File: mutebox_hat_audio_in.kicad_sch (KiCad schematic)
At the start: 23 parts, among them J1 GPIO, U1 CAT24C256, U2 74LVC157, U3 PCM1862DBT

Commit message: Fixed some connections and global labels
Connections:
- net GPIO18/PCM.CLK is gone; now on net I2S_BCLK: J1.12 (Pin_12), U2.4 (Za)
- net ADC_SDOUT: now also U2.10 (I1c)
- net GND: no longer U2.10 (I1c), U2.6 (I1b)
- net GPIO24: no longer U2.1 (S)
- net I2S_BCLK: no longer U2.2 (I0a), U3.17 (BCK)
- net I2S_LRCLK: now also U2.7 (Zb); no longer U2.5 (I0b), U3.16 (LRCK)
- net I2S_SDIN: now also J1.35 (Pin_35); no longer U2.3 (I1a)
- removed net GPIO19/PCM.FS: J1.35 (Pin_35), U2.7 (Zb)
- net GPIO20/PCM.DIN renamed I2S_DOUT
- net GPIO23_OPT_LOCK renamed SRC_SEL
- net SRC_SEL: now also U2.1 (S)
- net SPDIF_SDOUT renamed TOSLINK_DOUT
- new net ADC_BCLK: U2.3 (I1a), U3.17 (BCK)
- new net ADC_LRCLK: U2.6 (I1b), U3.16 (LRCK)
- new net TOSLINK_BCLK: U2.2 (I0a)
- new net TOSLINK_LRCK: U2.5 (I0b)
- no-connect marks 32 -> 33
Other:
- moved on the sheet: C8, J_R_IN1

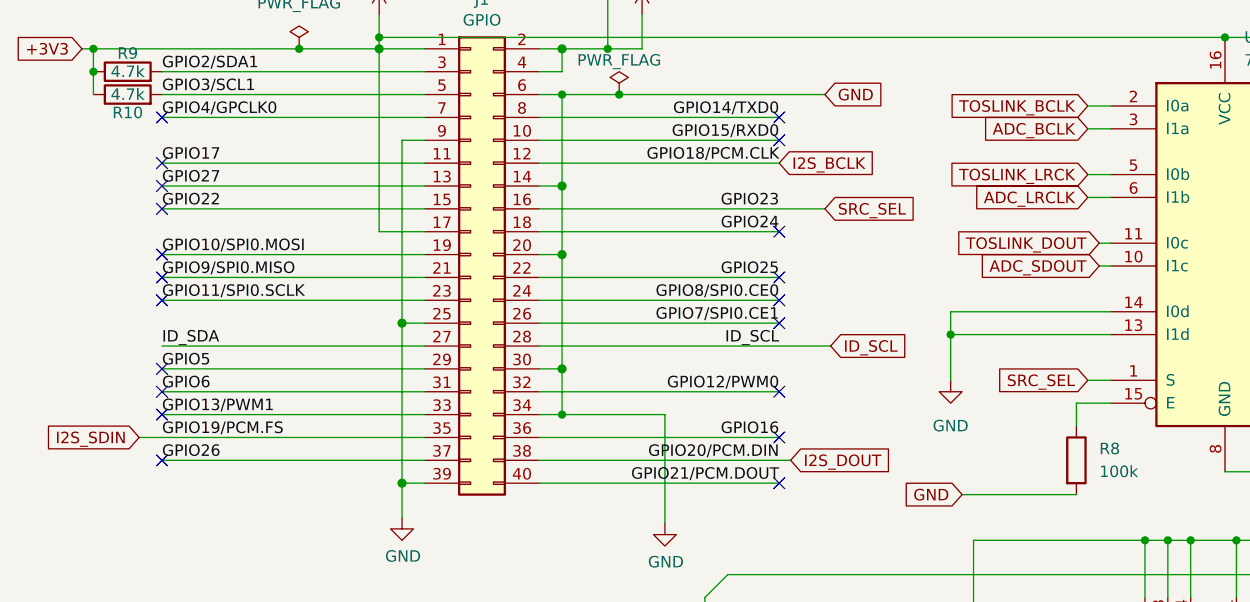
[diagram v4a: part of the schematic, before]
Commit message: Fixed power/caps for TOSLINK.  Got ERC down to warnings
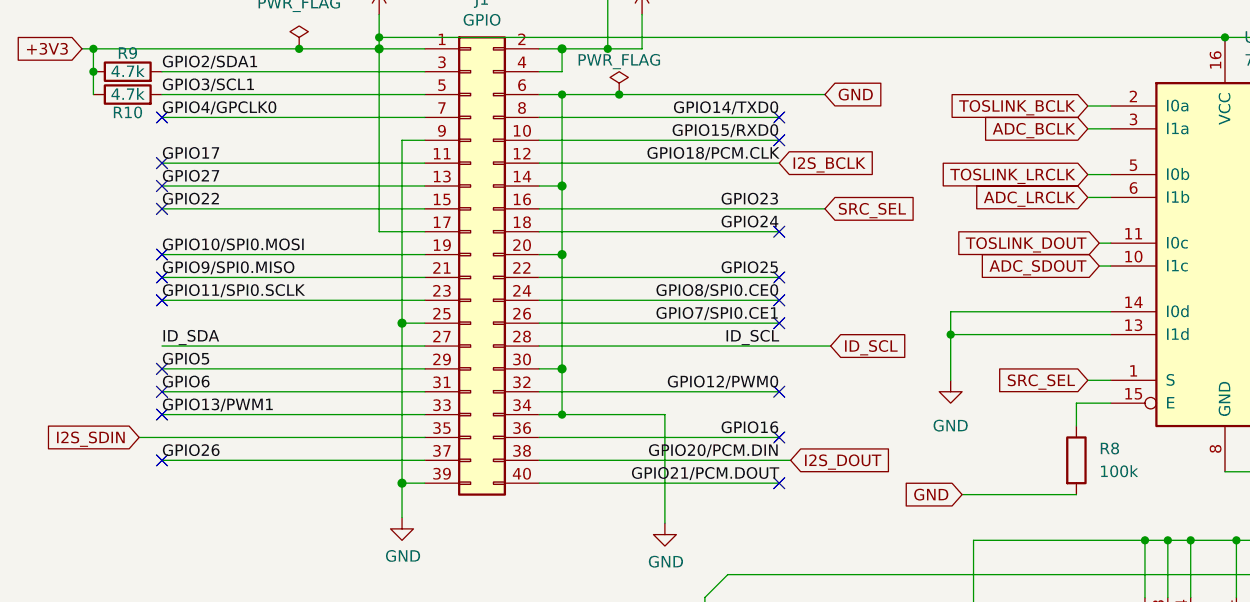
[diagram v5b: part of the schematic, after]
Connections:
- net TOSLINK_LRCK renamed TOSLINK_LRCLK
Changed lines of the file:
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@@
+	(wire
+		(pts
+			(xy 29.21 71.12) (xy 60.96 71.12)
+		)
+		(stroke
+			(width 0)
+			(type default)
+		)
+	)
 	(wire
 		(pts
@@
 		(pts
 			(xy 161.29 109.22) (xy 166.37 109.22)
-		)
-		(stroke
-			(width 0)
-			(type default)
-		)
-	)
-	(wire
-		(pts
-			(xy 29.21 71.12) (xy 60.96 71.12)
 		)
 		(stroke
@@
 		)
 	)
-	(label "GPIO19{slash}PCM.FS"
-		(at 31.75 71.12 0)
-		(effects
-			(font
-				(size 1.27 1.27)
-			)
-			(justify left bottom)
-		)
-	)
 	(label "GPIO10{slash}SPI0.MOSI"
 		(at 31.75 50.8 0)
@@
 		)
 	)
-	(global_label "TOSLINK_LRCK"
+	(global_label "TOSLINK_LRCLK"
 		(shape input)
 		(at 134.62 41.91 180)
@@
 		)
 		(property "Intersheetrefs" "${INTERSHEET_REFS}"
-			(at 151.247 41.91 0)
-			(effects
-				(font
-					(size 1.27 1.27)
-				)
-				(justify left)
-				(hide yes)
-			)
+			(at 116.9649 41.91 0)
+			(effects
+				(font
+					(size 1.27 1.27)
+				)
+				(justify right)
+				(hide yes)
+			)

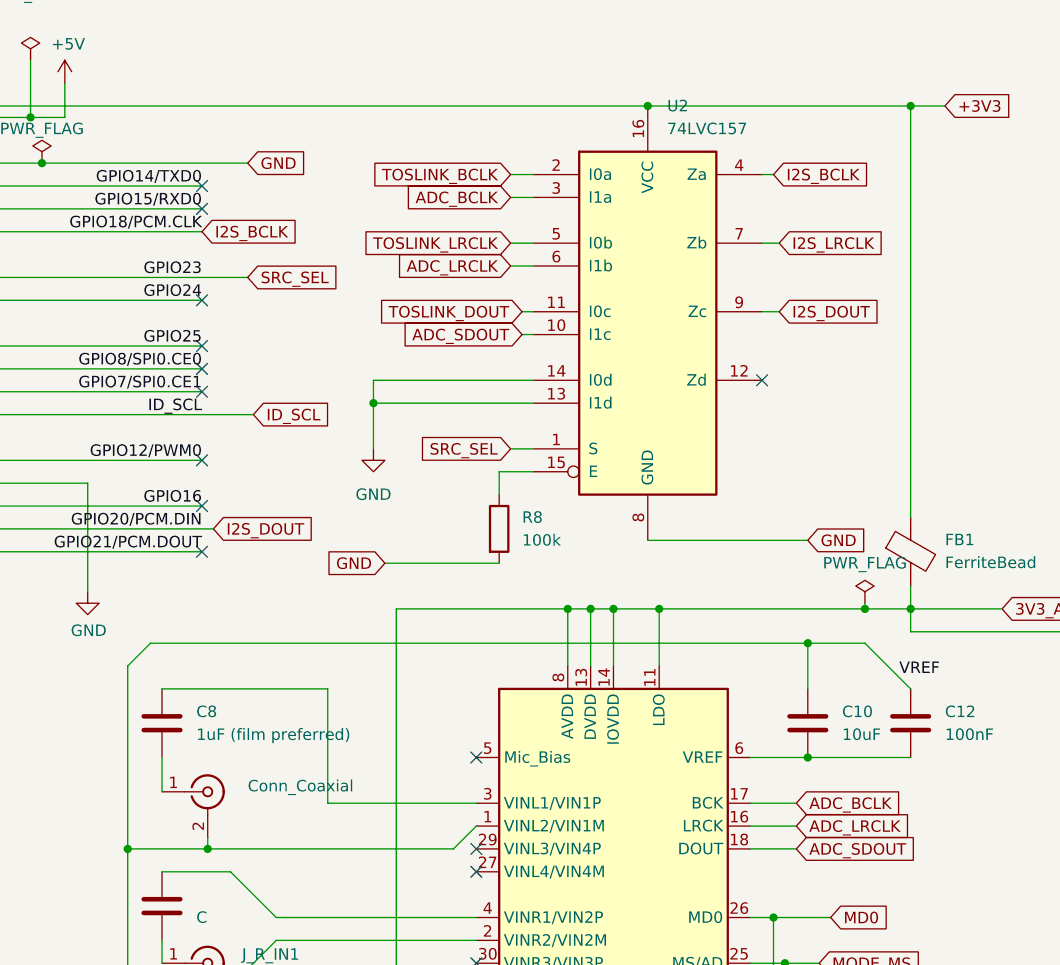
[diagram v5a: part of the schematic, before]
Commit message: Assigned footprints that were missing
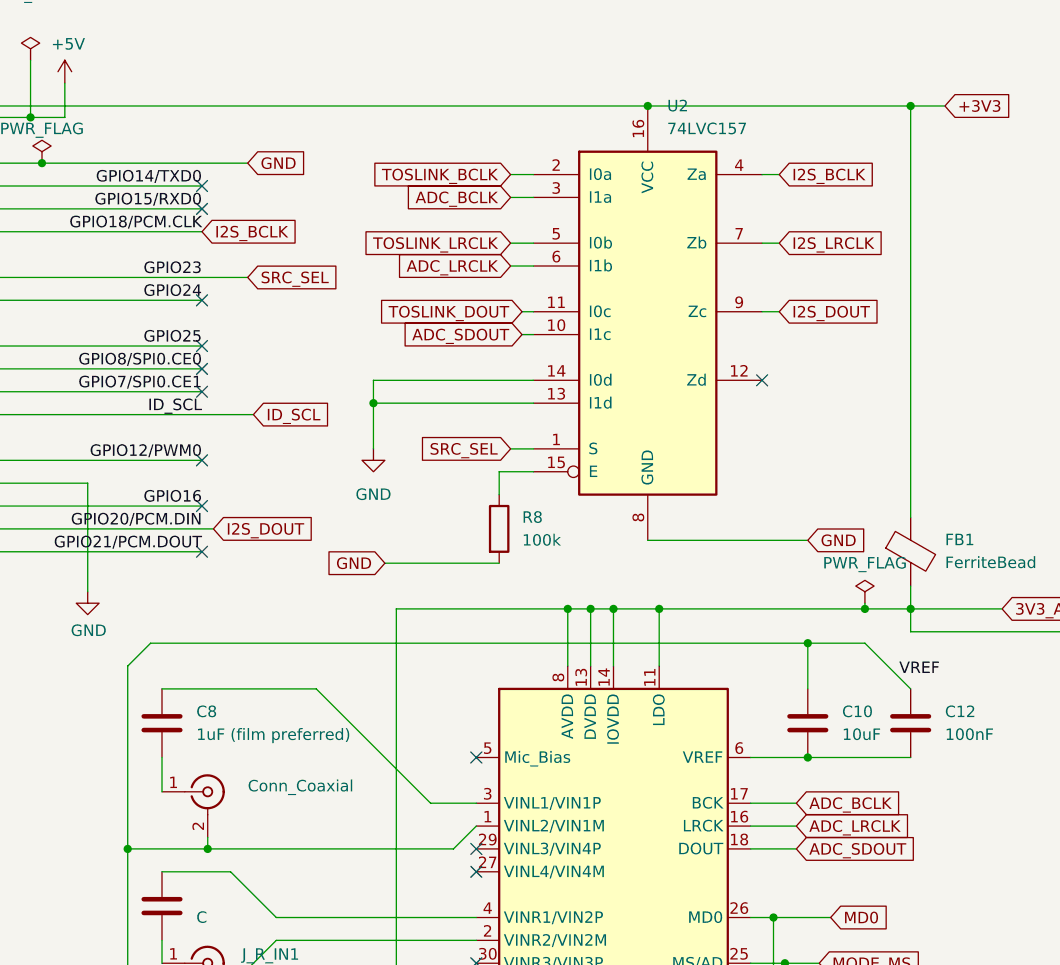
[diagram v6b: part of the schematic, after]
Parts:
- JP1: footprint (none) -> Connector_PinHeader_2.54mm:PinHeader_1x02_P2.54mm_Vertical
- J_L_IN1, J_R_IN1: footprint (none) -> Connector_Coaxial:SMA_Amphenol_901-143_Horizontal
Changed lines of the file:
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@@
 	(wire
 		(pts
-			(xy 95.885 91.44) (xy 114.3 91.44)
-		)
-		(stroke
-			(width 0)
-			(type default)
-		)
-	)
-	(wire
-		(pts
 			(xy 22.86 27.94) (xy 24.13 27.94)
 		)
@@
 	(wire
 		(pts
-			(xy 114.3 104.14) (xy 130.81 104.14)
-		)
-		(stroke
-			(width 0)
-			(type default)
-		)
-	)
-	(wire
-		(pts
 			(xy 135.89 49.53) (xy 137.16 49.53)
 		)
@@
 	(wire
 		(pts
-			(xy 162.56 34.29) (xy 163.83 34.29)
+			(xy 162.56 34.29) (xy 164.465 34.29)
 		)
 		(stroke
@@
 	(wire
 		(pts
-			(xy 114.3 91.44) (xy 114.3 104.14)
+			(xy 181.61 130.81) (xy 181.61 142.24)
 		)
 		(stroke
@@
 	(wire
 		(pts
-			(xy 181.61 130.81) (xy 181.61 142.24)
+			(xy 76.2 68.58) (xy 73.66 68.58)
 		)
 		(stroke
 			(width 0)
-			(type default)
+			(type solid)
 		)
 	)
 	(wire
 		(pts
-			(xy 76.2 68.58) (xy 73.66 68.58)
+			(xy 113.03 91.44) (xy 125.73 104.14)
 		)
 		(stroke
 			(width 0)
-			(type solid)
+			(type default)
 		)
 	)
@@
 	(wire
 		(pts
+			(xy 125.73 104.14) (xy 130.81 104.14)
+		)
+		(stroke
+			(width 0)
+			(type default)
+		)
+	)
+	(wire
+		(pts
 			(xy 163.83 132.08) (xy 187.96 132.08)
 		)
@@
 	(wire
 		(pts
+			(xy 95.885 91.44) (xy 113.03 91.44)
+		)
+		(stroke
+			(width 0)
+			(type default)
+		)
+	)
+	(wire
+		(pts
 			(xy 182.88 26.67) (xy 179.07 26.67)
 		)
@@
 	(global_label "I2S_BCLK"
 		(shape input)
-		(at 163.83 34.29 0)
+		(at 164.465 34.29 0)
 		(fields_autoplaced yes)
 		(effects
@@
 		)
 		(property "Intersheetrefs" "${INTERSHEET_REFS}"
-			(at 175.7398 34.29 0)
+			(at 176.3748 34.29 0)
 			(effects
 				(font
@@
 			)
 		)
-		(property "Footprint" ""
+		(property "Footprint" "Connector_PinHeader_2.54mm:PinHeader_1x02_P2.54mm_Vertical"
 			(at 96.52 180.34 0)
 			(effects
@@
 			)
 		)
-		(property "Footprint" ""
+		(property "Footprint" "Connector_Coaxial:SMA_Amphenol_901-143_Horizontal"
 			(at 100.965 102.87 0)
 			(effects
@@
 			)
 		)
-		(property "Footprint" ""
+		(property "Footprint" "Connector_Coaxial:SMA_Amphenol_901-143_Horizontal"
 			(at 100.965 121.92 0)
 			(effects
